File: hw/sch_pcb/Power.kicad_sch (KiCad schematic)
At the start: 23 parts, among them U1 NCP1117ST33, U11 TPS563249

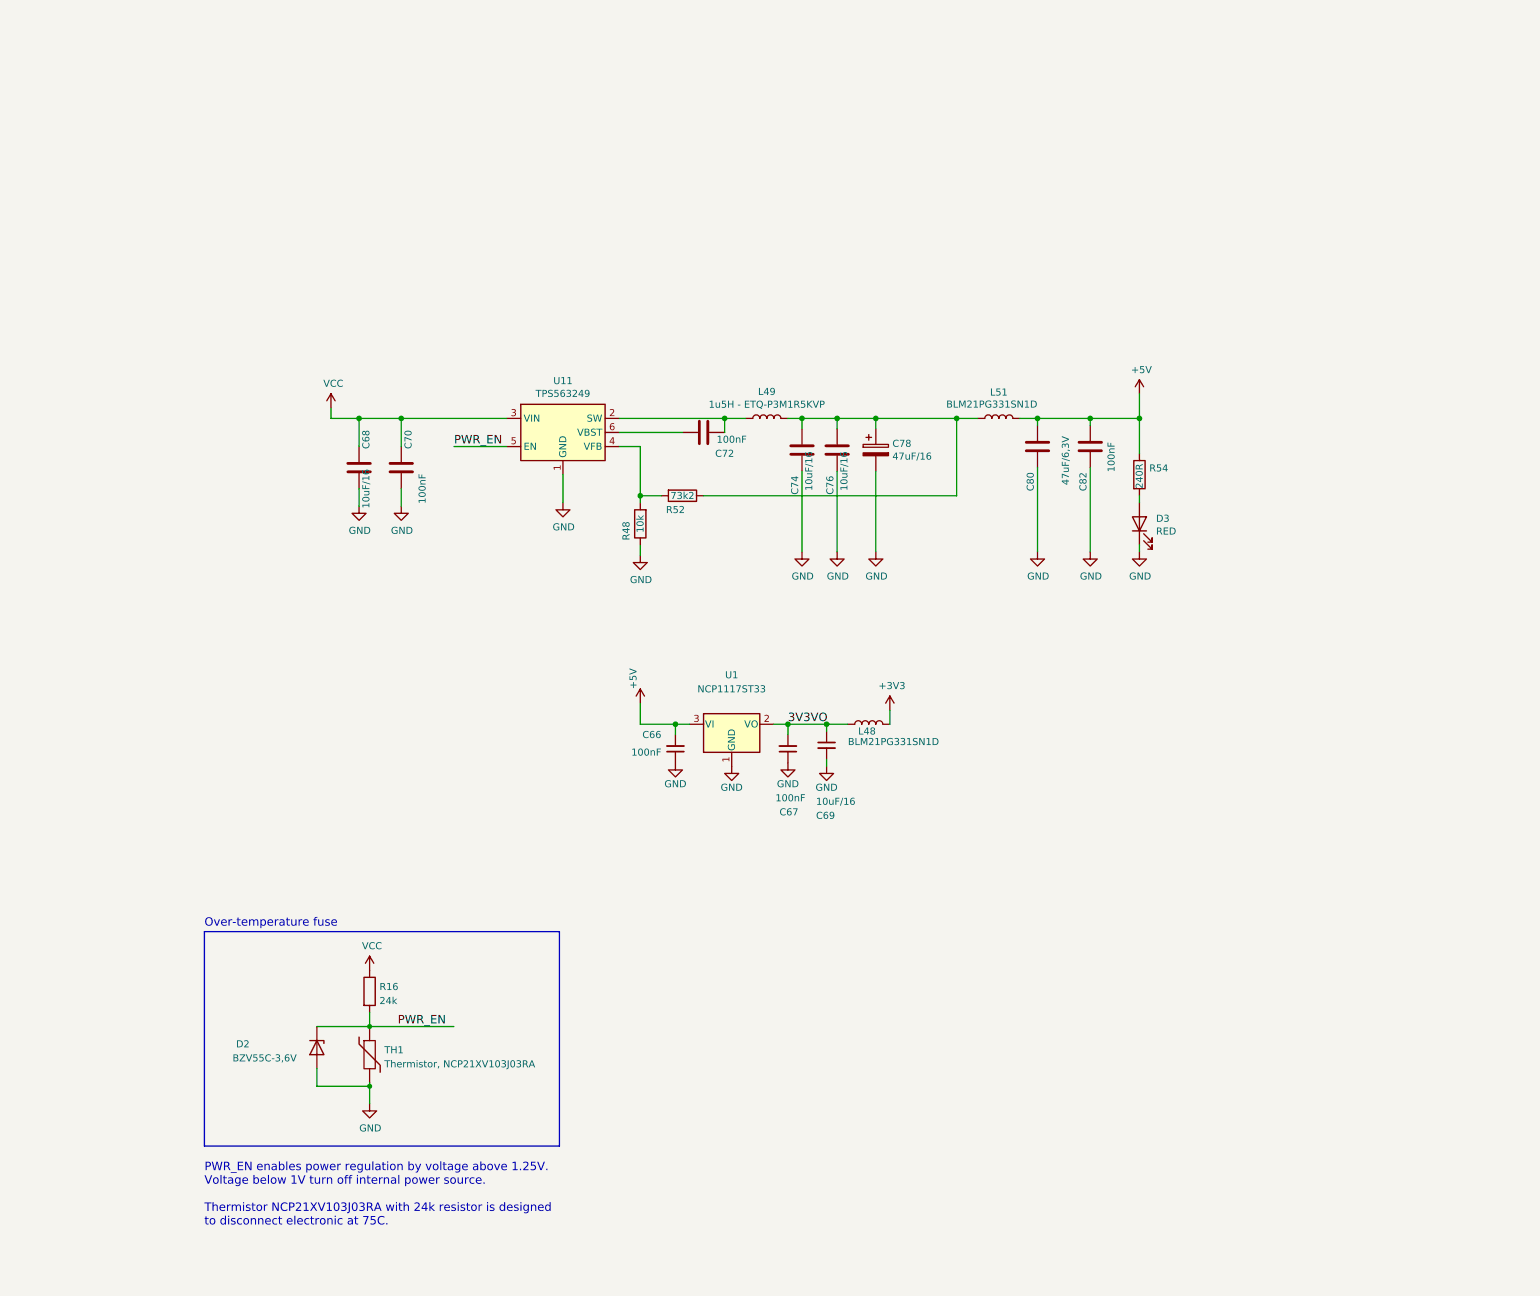
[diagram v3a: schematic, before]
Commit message: rozpracovani #11 (menic na 5 a 3v3)
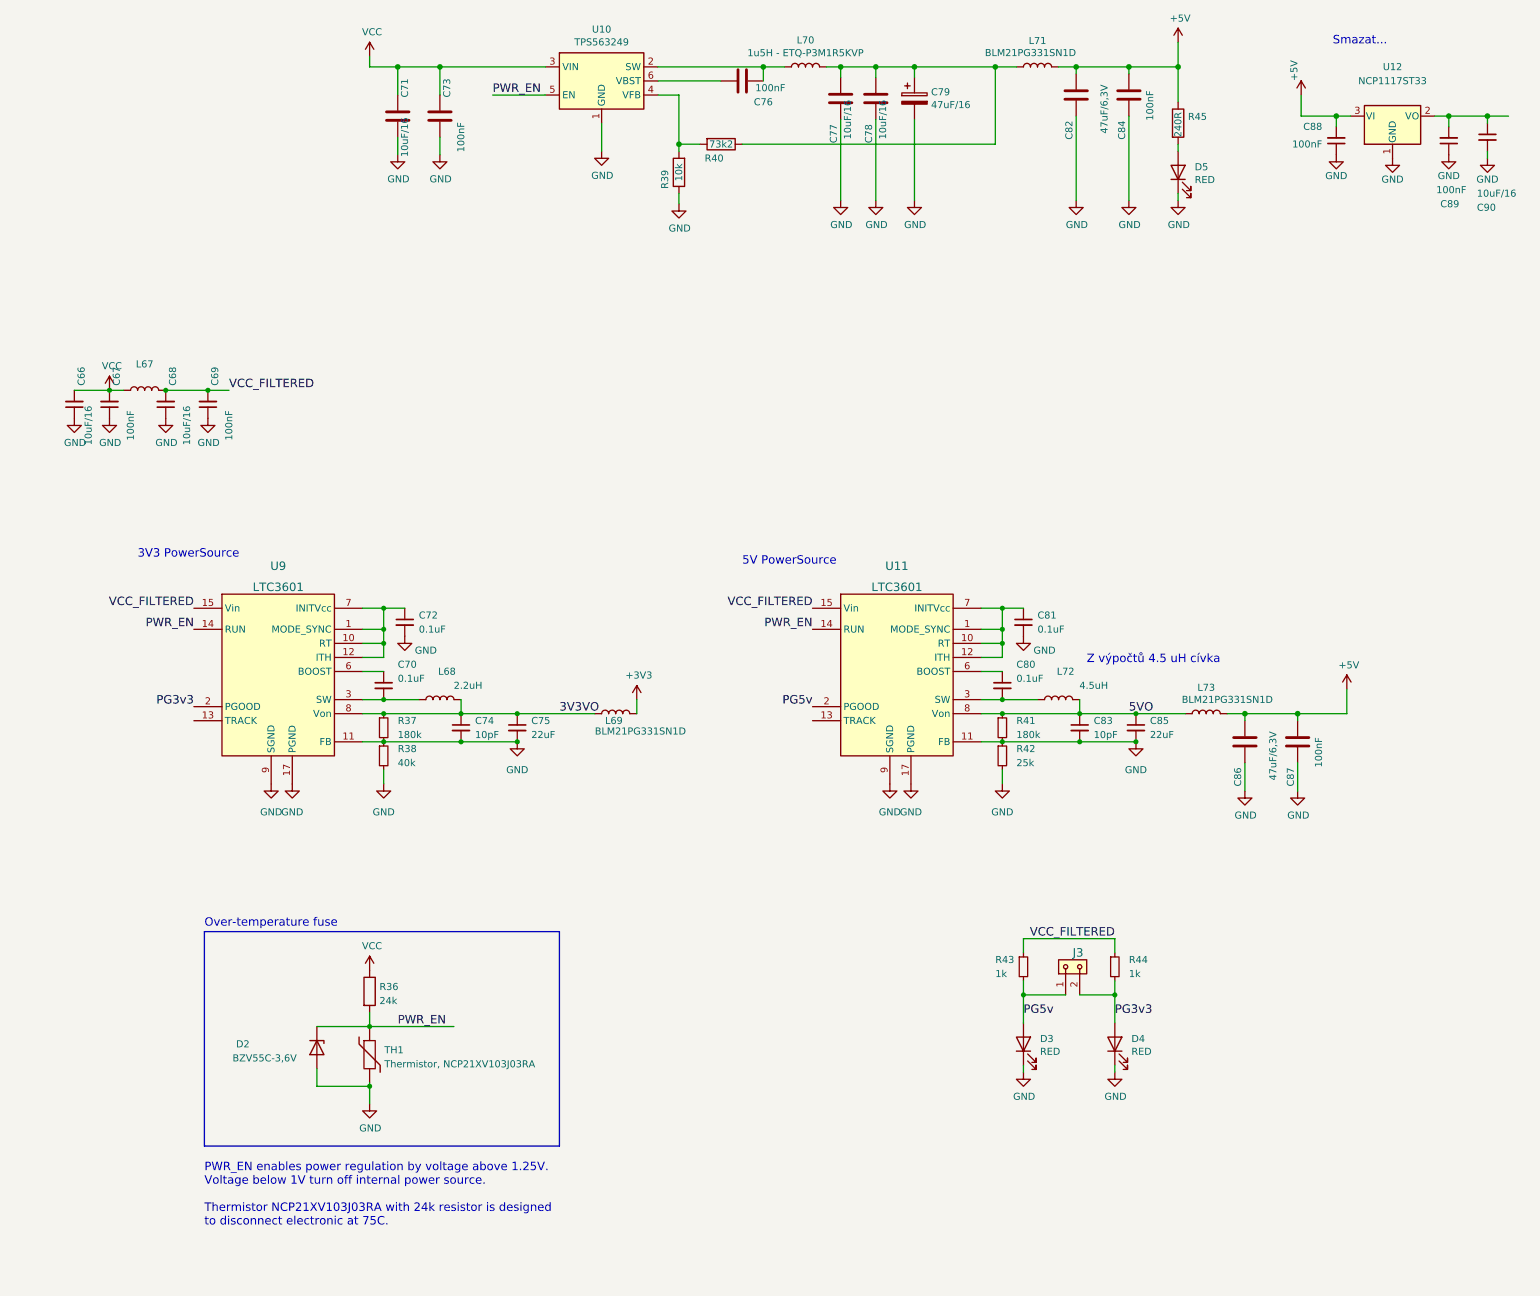
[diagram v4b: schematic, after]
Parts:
- added C66, C68: 10uF/16, Capacitor_SMD:C_0805_2012Metric, symbol Device:C_Small
- added C67, C69: 100nF, Capacitor_SMD:C_0603_1608Metric, symbol Device:C_Small
- added C70, C72, C80, C81: 0.1uF, symbol Device:C_Small
- added C74, C83: 10pF, symbol Device:C_Small
- added C75, C85: 22uF, symbol Device:C_Small
- added C86: 47uF/6,3V, Capacitor_SMD:C_0805_2012Metric, symbol Device:C
- added C87: 100nF, Capacitor_SMD:C_0603_1608Metric, symbol Device:C
- added D3, D4: RED, Mlab_D:LED_1206, symbol Device:LED
- added J3: HEADER_1x02, Mlab_Pin_Headers:Straight_1x02, symbol MLAB_HEADER:HEADER_1x02
- added L67: (no value), symbol Device:L
- added L68: 2.2uH, symbol Device:L
- added L72: 4.5uH, symbol Device:L
- added L73: BLM21PG331SN1D, Inductor_SMD:L_0805_2012Metric_Pad1.15x1.40mm_HandSolder, symbol Device:L
- added R37, R41: 180k, Resistor_SMD:R_0603_1608Metric, symbol Device:R_Small
- added R38: 40k, Resistor_SMD:R_0603_1608Metric, symbol Device:R_Small
- added R42: 25k, Resistor_SMD:R_0603_1608Metric, symbol Device:R_Small
- added R43, R44: 1k, Resistor_SMD:R_0603_1608Metric, symbol Device:R_Small
- added U11, U9: LTC3601, Package_DFN_QFN:QFN-16-1EP_3x3mm_P0.5mm_EP1.7x1.7mm_ThermalVias, symbol MLAB_IO:LTC3601
- renumbered C68 to C71, C70 to C73, C72 to C76, C74 to C77, C76 to C78, C78 to C79, C80 to C82, C82 to C84, C66 to C88, C67 to C89, C69 to C90, D3 to D5, L48 to L69, L49 to L70, L51 to L71, R16 to R36, R48 to R39, R52 to R40, R54 to R45, U11 to U10, U1 to U12
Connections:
- net +5V: now also C86.2, C87.2, L73.2
- net 3V3VO: now also C74.1, C75.1, L68.2, R37.1, U9.8 (Von); no longer C89.2, C90.1, U12.2 (VO)
- net GND: now also C66.1, C67.1, C68.1, C69.1, C72.2, C74.2, C75.2, C81.2, C83.2, C85.2, C86.1, C87.1, D3.1 (K), D4.1 (K), R37.2, R38.1, R38.2, R41.2, R42.1, R42.2, U11.11 (FB), U11.17 (PGND), U11.9 (SGND), U9.11 (FB), U9.17 (PGND), U9.9 (SGND)
- net PWR_EN: now also U11.14 (RUN), U9.14 (RUN)
- net VCC: now also C66.2, C67.2, L67.1
- new net: C89.2, C90.1, U12.2 (VO)
- new net: C70.1, U9.6 (BOOST)
- new net: C70.2, L68.1, U9.3 (SW), U9.4 (SW)
- new net: C72.1, U9.1 (MODE_SYNC), U9.10 (RT), U9.12 (ITH), U9.7 (INITVcc)
- new net: C80.1, U11.6 (BOOST)
- new net: C80.2, L72.1, U11.3 (SW), U11.4 (SW)
- new net: C81.1, U11.1 (MODE_SYNC), U11.10 (RT), U11.12 (ITH), U11.7 (INITVcc)
- new net 5VO: C83.1, C85.1, L72.2, L73.1, R41.1, U11.8 (Von)
- new net PG3v3: D4.2 (A), J3.2, R44.2, U9.2 (PGOOD)
- new net PG5v: D3.2 (A), J3.1, R43.2, U11.2 (PGOOD)
- new net VCC_FILTERED: C68.2, C69.2, L67.2, R43.1, R44.1, U11.15 (Vin), U11.16 (Vin), U9.15 (Vin), U9.16 (Vin)
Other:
- note added: "3V3 PowerSource"
- note added: "5V PowerSource"
- note added: "Smazat..."
- note added: "Z výpočtů 4.5 uH cívka"
- moved on the sheet: C71, C73, C76, C77, C78, C79, C82, C84, C88, C89, C90, D5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

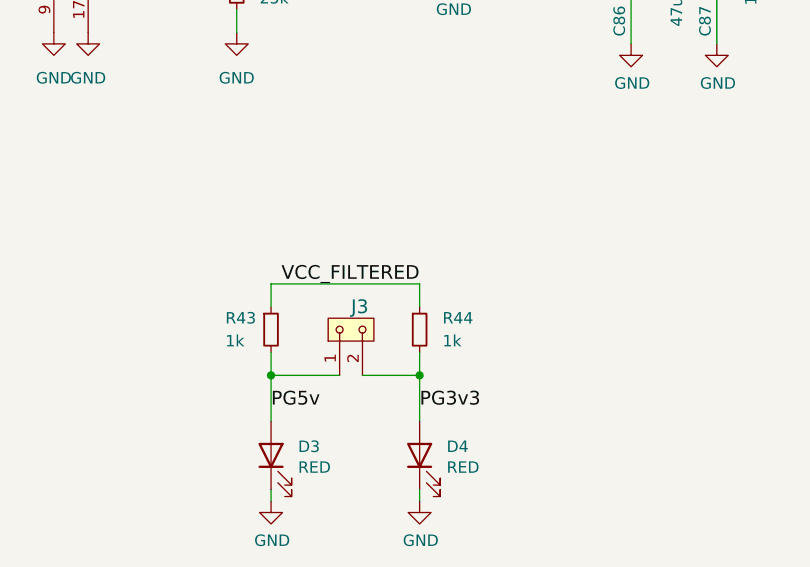
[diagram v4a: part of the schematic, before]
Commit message: uprava ledek napajeni #11
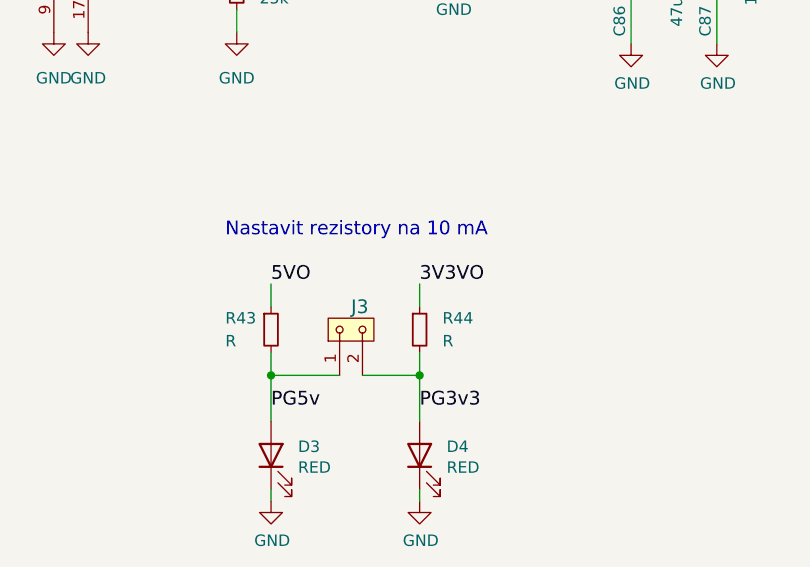
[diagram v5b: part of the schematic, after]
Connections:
- net 3V3VO: now also R44.1
- net 5VO: now also R43.1
- net VCC_FILTERED: no longer R43.1, R44.1
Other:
- note added: "Nastavit rezistory na 10 mA"
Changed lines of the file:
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@@
     (stroke (width 0) (type solid) (color 0 0 0 0))
-  )
-  (wire (pts (xy 195.58 125.73) (xy 212.09 125.73))
-    (stroke (width 0) (type default) (color 0 0 0 0))
   )
   (wire (pts (xy 168.91 -31.75) (xy 175.895 -31.75))
@@
     (effects (font (size 1.524 1.524)) (justify left bottom))
   )
+  (text "Nastavit rezistory na 10 mA" (at 190.5 120.65 0)
+    (effects (font (size 1.524 1.524)) (justify left bottom))
+  )
   (text "Over-temperature fuse" (at 47.625 123.825 0)
     (effects (font (size 1.524 1.524)) (justify left bottom))
@@
     (effects (font (size 1.524 1.524)) (justify left bottom))
   )
-  (label "VCC_FILTERED" (at 212.09 125.73 180)
-    (effects (font (size 1.524 1.524)) (justify right bottom))
+  (label "3V3VO" (at 212.09 125.73 0)
+    (effects (font (size 1.524 1.524)) (justify left bottom))
   )
   (label "PWR_EN" (at 45.72 69.85 180)
@@
   )
   (label "5VO" (at 214.63 85.09 0)
+    (effects (font (size 1.524 1.524)) (justify left bottom))
+  )
+  (label "5VO" (at 195.58 125.73 0)
     (effects (font (size 1.524 1.524)) (justify left bottom))
   )
@@
       (effects (font (size 1.27 1.27)) (justify left))
     )
-    (property "Value" "1k" (id 1) (at 190.5 132.08 0)
+    (property "Value" "R" (id 1) (at 190.5 132.08 0)
       (effects (font (size 1.27 1.27)) (justify left))
     )
@@
       (effects (font (size 1.27 1.27)) (justify left))
     )
-    (property "Value" "1k" (id 1) (at 214.63 132.0799 0)
-      (effects (font (size 1.27 1.27)) (justify left))
-    )
+    (property "Value" "R" (id 1) (at 214.63 132.0799 0)
+      (effects (font (size 1.27 1.27)) (justify left))
+    )
